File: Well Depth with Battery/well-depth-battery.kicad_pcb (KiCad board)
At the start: 2 copper layers, 30 x 60 mm, 63 parts, among them J1 Conn_01x02, J2 Conn_01x02, J3 Conn_02x04_Odd_Even, J5 Conn_01x04, J6 Conn_01x04, Q1 Q_NMOS_GSD, Q2 Q_PMOS_GSD, U1 LM358, U2 LM358, U3 TL431DBZ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

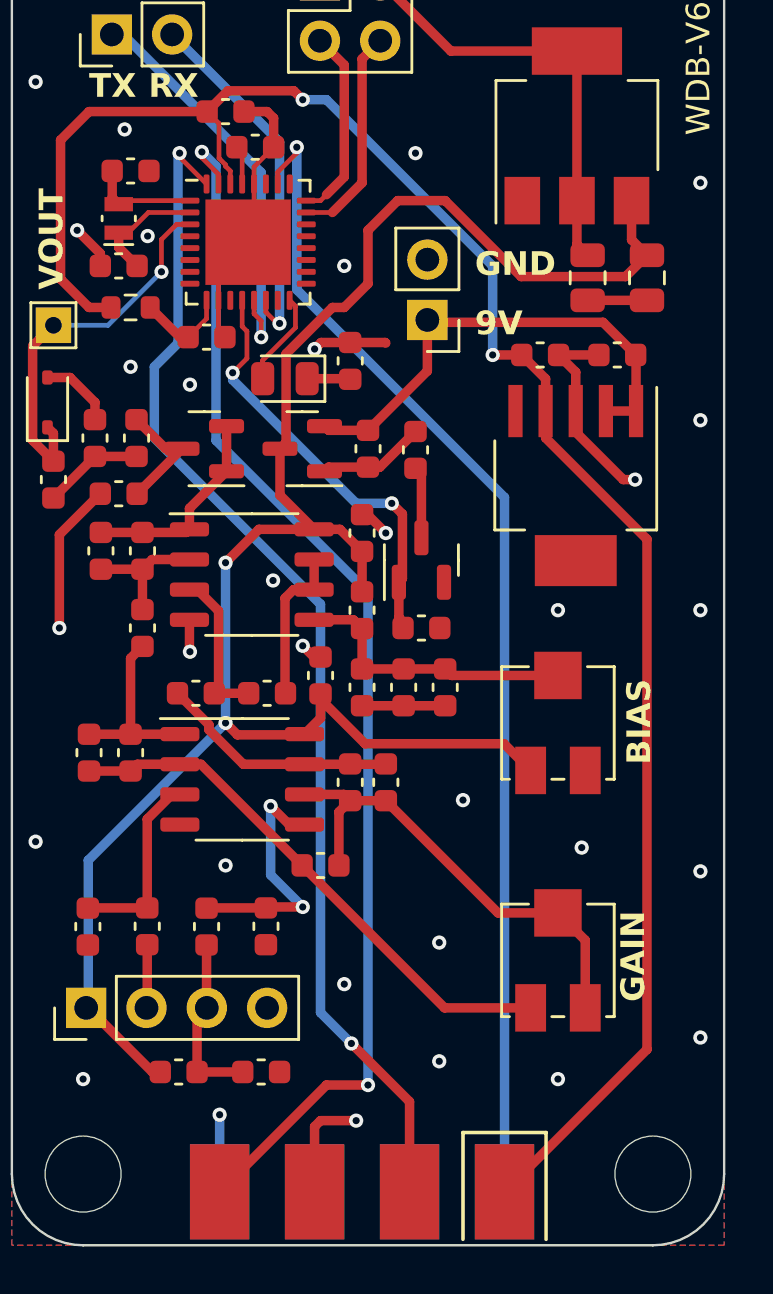
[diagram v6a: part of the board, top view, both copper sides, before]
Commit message: Fix prog connector
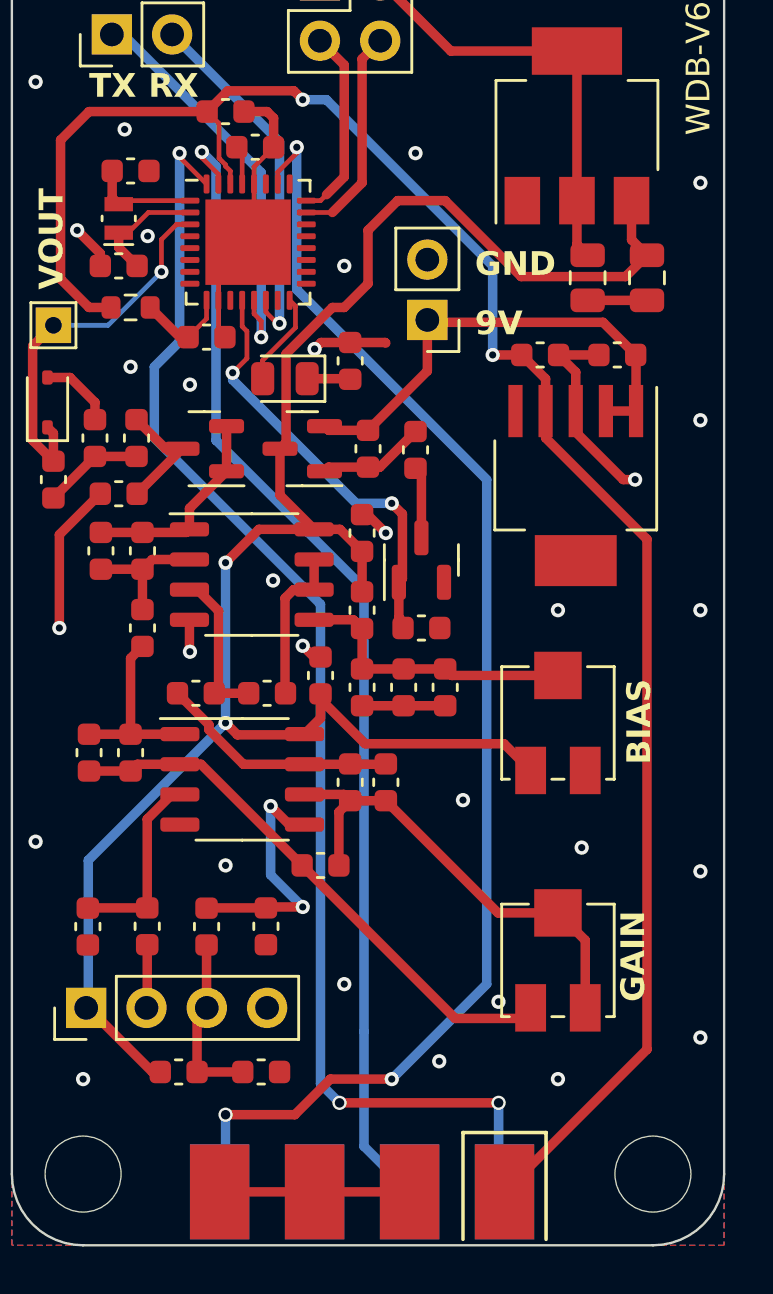
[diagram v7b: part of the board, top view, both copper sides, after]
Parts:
- J3: footprint EWB:CardEdge_Prog -> MyParts:CardEdge_Prog
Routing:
- net /~{SRST}: track 49.5 -> 57.1 mm, vias 1 -> 3
- net /SWDIO: track 50.4 -> 56.0 mm, vias 2 -> 3
- net /SWCLK: track 52.0 -> 49.1 mm, vias 2 -> 1
- net GND: track 52.3 -> 52.4 mm, vias 35 -> 33
